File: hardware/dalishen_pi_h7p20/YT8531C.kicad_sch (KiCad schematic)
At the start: 49 parts, among them J10 RJ45_HR911130A, U1 YT8531C, Y2 NC

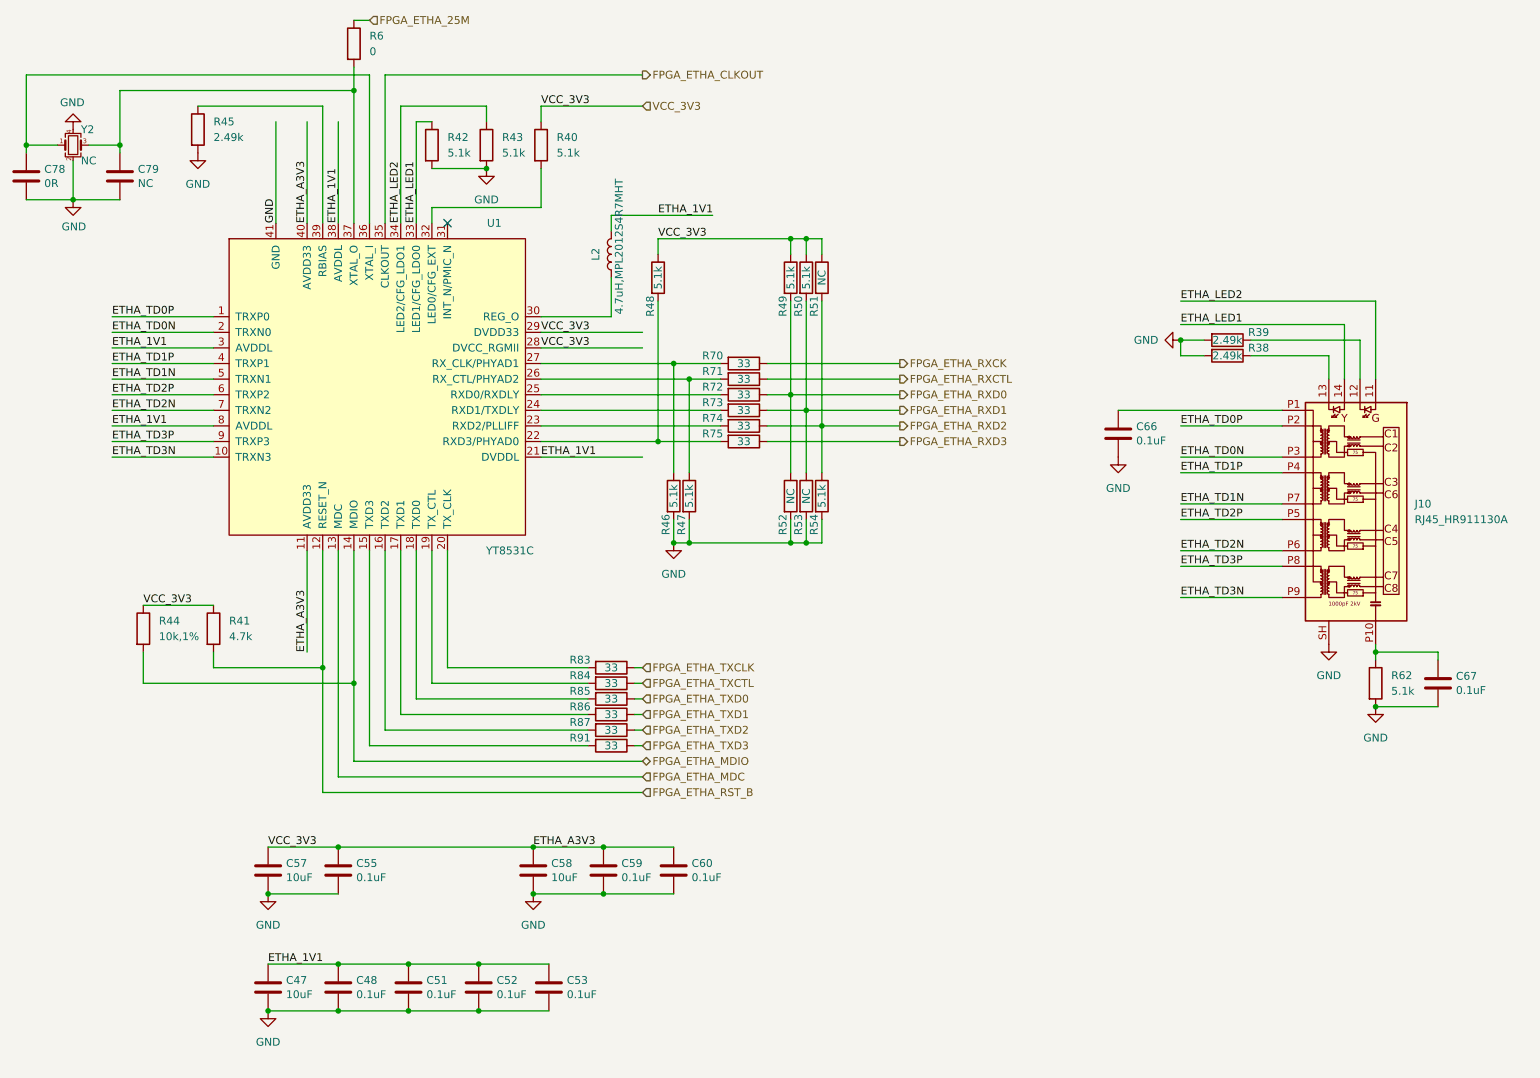
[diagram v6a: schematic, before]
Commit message: [dalishen_pi_h7p20] 生成方波
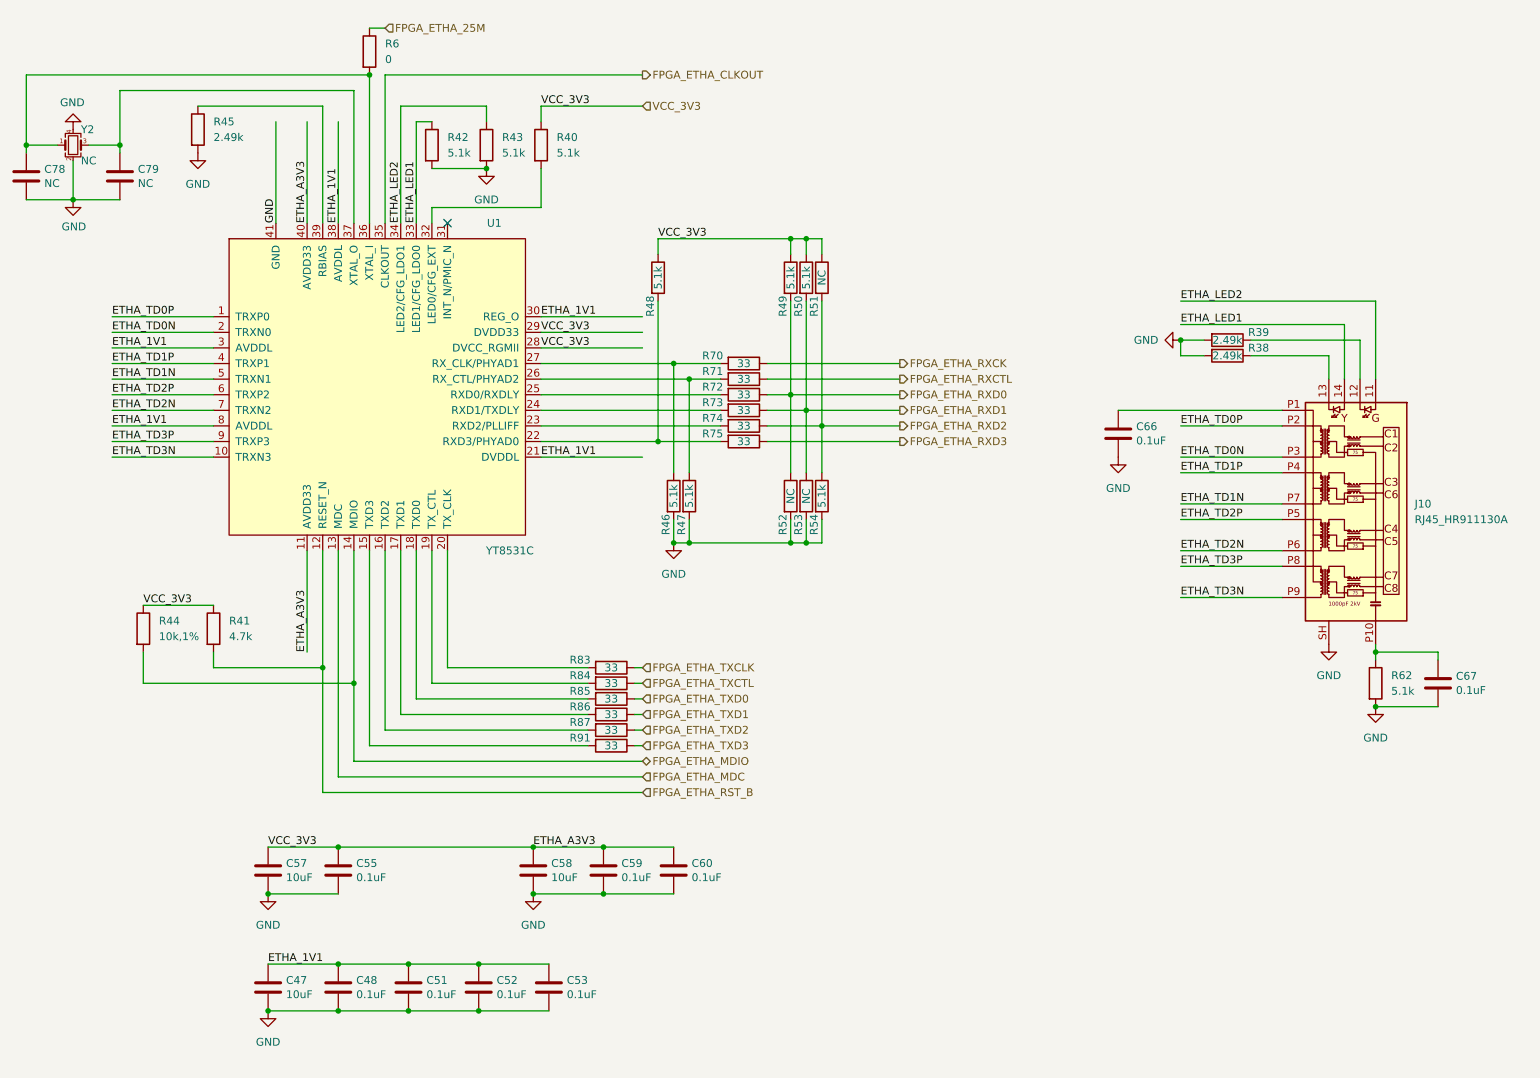
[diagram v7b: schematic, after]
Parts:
- removed L2: 4.7uH,MPL2012S4R7MHT, Inductor_SMD:L_0805_2012Metric, symbol Device:L
- C78: value 0R -> NC
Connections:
- net ETHA_1V1: now also U1.30 (REG_O)
- net at C78.2, U1.36 (XTAL_I), Y2.1: now also R6.2
- net at C79.2, U1.37 (XTAL_O), Y2.3: no longer R6.2
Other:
- moved on the sheet: R6
